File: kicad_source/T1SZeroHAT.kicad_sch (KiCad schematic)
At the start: 35 parts, among them CN1 RASPI-IO, CN2 XY2500R-F-3.81-4P, CN3 SM04B-GHS-TB, CN4 SM04B-GHS-TB, SW1 SS-3235S-L3, U1 MCP2518FDT-E/SL, U2 TCAN332GDR, Y1 X1E0000210808

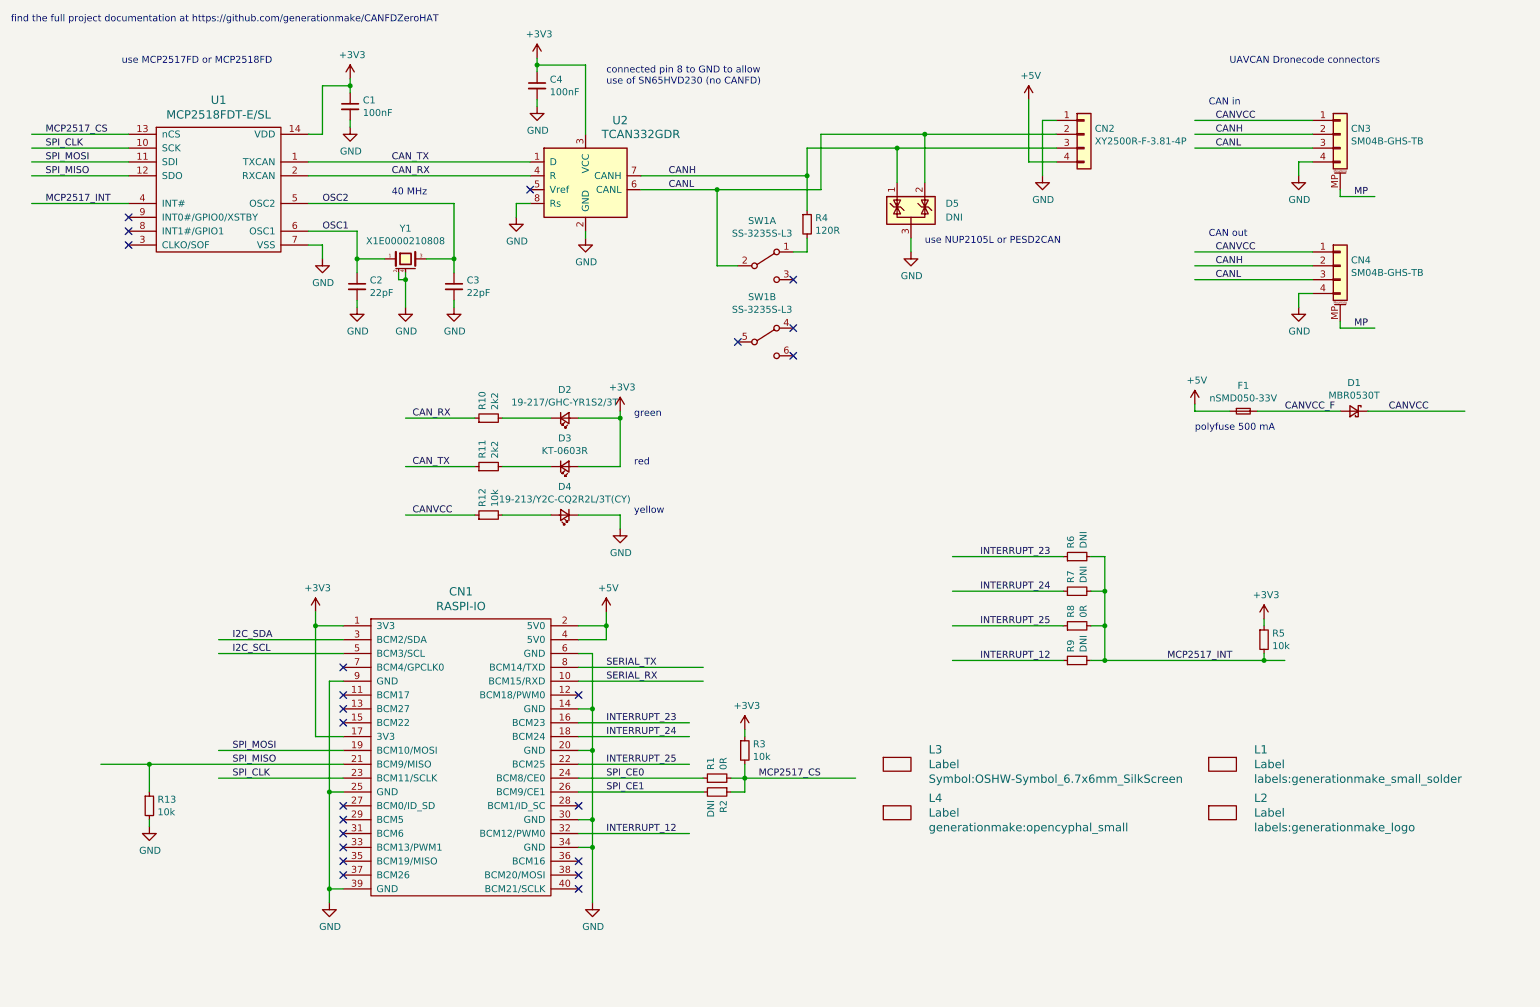
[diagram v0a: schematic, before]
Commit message: added LAN8651 to the schematic
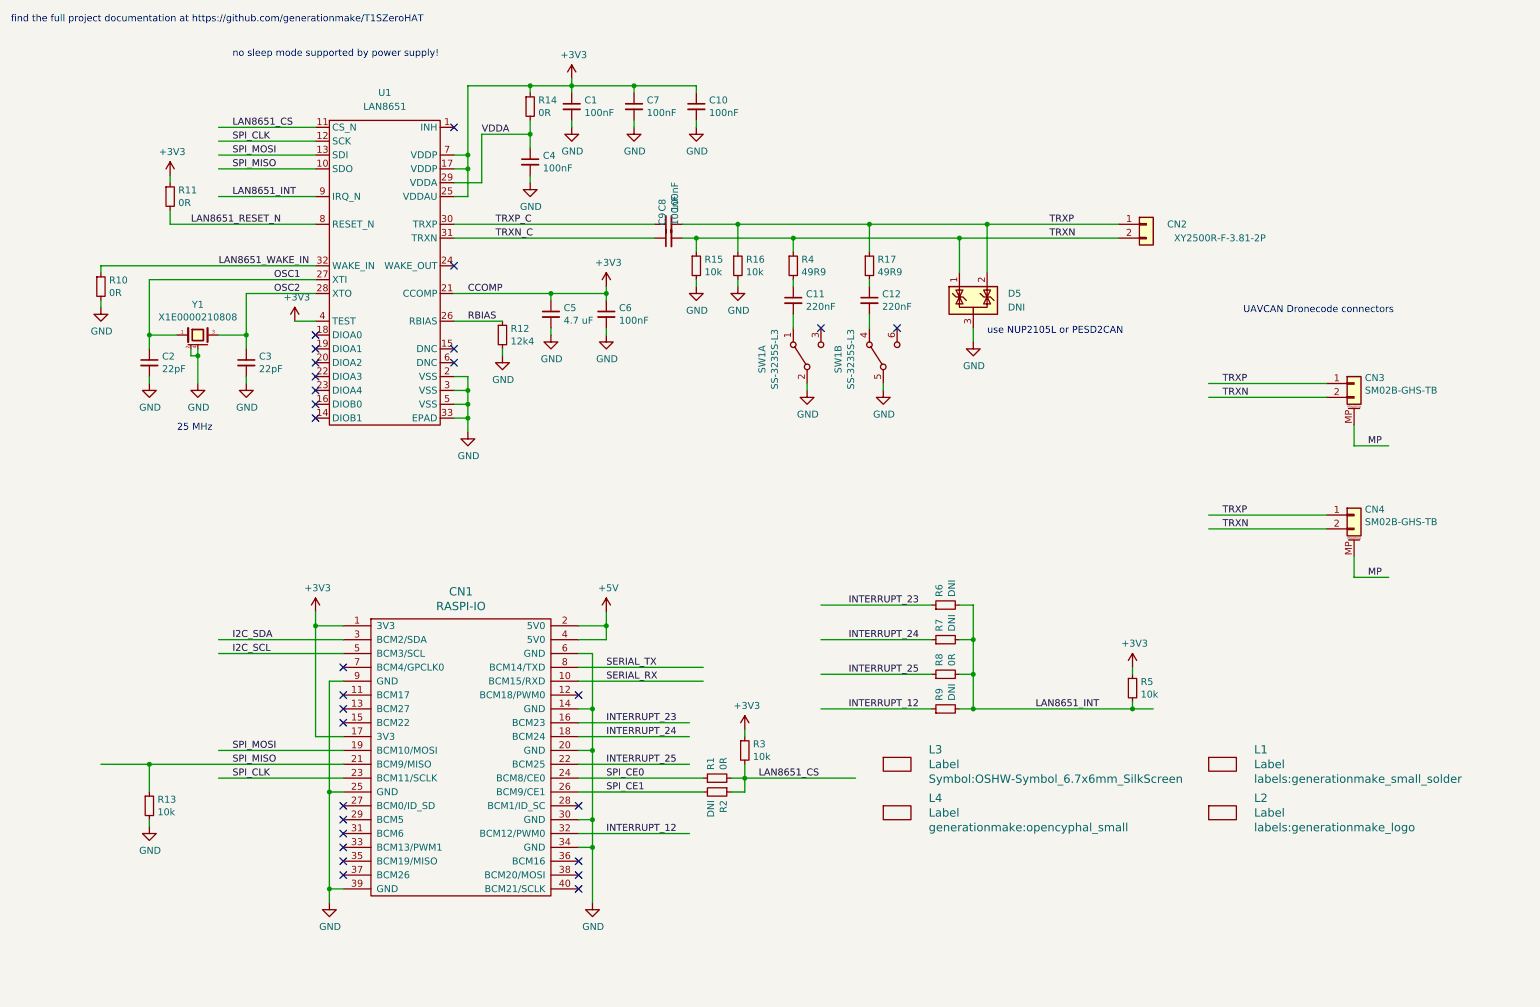
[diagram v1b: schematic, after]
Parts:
- removed D1: MBR0530T, Diode_SMD:D_SOD-123, symbol Device:D_Schottky_Small
- removed D2: 19-217/GHC-YR1S2/3T, LED_SMD:LED_0603_1608Metric, symbol Device:LED_Small
- removed D3: KT-0603R, LED_SMD:LED_0603_1608Metric, symbol Device:LED_Small
- removed D4: 19-213/Y2C-CQ2R2L/3T(CY), LED_SMD:LED_0603_1608Metric, symbol Device:LED_Small
- removed F1: nSMD050-33V, Fuse:Fuse_1206_3216Metric, symbol Device:Fuse_Small
- removed U1: MCP2518FDT-E/SL, Package_SO:SOIC-14_3.9x8.7mm_P1.27mm, symbol CANFDZeroHAT-rescue:MCP2517FD-IC_transceiver_can
- removed U2: TCAN332GDR, Package_SO:SOIC-8_3.9x4.9mm_P1.27mm, symbol Interface_CAN_LIN:SN65HVD230
- added C10, C6, C7, C8, C9: 100nF, Capacitor_SMD:C_0603_1608Metric, symbol Device:C_Small
- added C11, C12: 220nF, Capacitor_SMD:C_0603_1608Metric, symbol Device:C_Small
- added C5: 4.7 uF, Capacitor_SMD:C_0603_1608Metric, symbol Device:C_Small
- added R14: 0R, Resistor_SMD:R_0603_1608Metric, symbol Device:R_Small
- added R15, R16: 10k, Resistor_SMD:R_0603_1608Metric, symbol Device:R_Small
- added R17: 49R9, Resistor_SMD:R_0603_1608Metric, symbol Device:R_Small
- added U1: LAN8651, Package_DFN_QFN:QFN-32-1EP_5x5mm_P0.5mm_EP3.45x3.45mm, symbol generationmake:LAN8651
- CN2: value XY2500R-F-3.81-4P -> XY2500R-F-3.81-2P; footprint Connector_Phoenix_MC:PhoenixContact_MC_1,5_4-G-3.81_1x04_P3.81mm_Horizontal -> Connector_Phoenix_MC:PhoenixContact_MC_1,5_2-G-3.81_1x02_P3.81mm_Horizontal; symbol Connector_Generic:Conn_01x04 -> Connector_Generic:Conn_01x02; LCSC C880583 -> (none)
- CN3, CN4: value SM04B-GHS-TB -> SM02B-GHS-TB; footprint Connector_JST:JST_GH_SM04B-GHS-TB_1x04-1MP_P1.25mm_Horizontal -> Connector_JST:JST_GH_SM02B-GHS-TB_1x02-1MP_P1.25mm_Horizontal; symbol Connector_Generic_MountingPin:Conn_01x04_MountingPin -> Connector_Generic_MountingPin:Conn_01x02_MountingPin; LCSC C189895 -> (none)
- R10, R11: value 2k2 -> 0R; LCSC C4190 -> C2889381
- R12: value 10k -> 12k4; LCSC C25804 -> (none)
- R4: value 120R -> 49R9; LCSC C22787 -> (none)
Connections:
- net CAN_TX is gone; now on net +3.3V: R11.1
- net +3.3V: now also C10.1, C5.1, C6.1, C7.1, R14.1, U1.17 (VDDP), U1.21 (CCOMP), U1.25 (VDDAU), U1.4 (TEST), U1.7 (VDDP); no longer C4.1
- net +5V: no longer CN2.4 (Pin_4)
- net GND: now also R10.2, R12.2, SW1.2 (B), SW1.5 (B), C10.2, C5.2, C6.2, C7.2, R15.2, R16.2, U1.2 (VSS), U1.3 (VSS), U1.33 (EPAD), U1.5 (VSS); no longer CN2.1 (Pin_1), CN3.4 (Pin_4), CN4.4 (Pin_4)
- net OSC1: now also U1.27 (XTI)
- net OSC2: now also U1.28 (XTO)
- net SPI_CLK: now also U1.12 (SCK)
- net SPI_MISO: now also U1.10 (SDO)
- net SPI_MOSI: now also U1.13 (SDI)
- net at R4.2: now also C11.1; no longer SW1.1 (A)
- net LAN8651_RESET_N: now reaches R11.2
- net LAN8651_RESET_N: now also U1.8 (RESET_N)
- net at SW1.4 (A): now also C12.2
- net CANH renamed TRXN
- net TRXN: now also CN2.2 (Pin_2), C9.2, R15.1; no longer CN2.3 (Pin_3)
- removed net CANL: CN2.2 (Pin_2), CN3.3 (Pin_3), CN4.3 (Pin_3), D5.2 (K), SW1.2 (B)
- net CANVCC renamed TRXP
- net TRXP: now also CN2.1 (Pin_1), D5.2 (K), C8.2, R16.1, R17.1; no longer R12.1
- net CAN_RX renamed LAN8651_WAKE_IN
- net LAN8651_WAKE_IN: now also U1.32 (WAKE_IN)
- net MCP2517_CS renamed LAN8651_CS
- net LAN8651_CS: now also U1.11 (CS_N)
- net MCP2517_INT renamed LAN8651_INT
- net LAN8651_INT: now also U1.9 (IRQ_N)
- new net: C11.2, SW1.1 (A)
- new net: C12.1, R17.2
- new net RBIAS: R12.1, U1.26 (RBIAS)
- new net TRXN_C: C9.1, U1.31 (TRXN)
- new net TRXP_C: C8.1, U1.30 (TRXP)
- new net VDDA: C4.1, R14.2, U1.29 (VDDA)
- no-connect marks 23 -> 28
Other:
- note added: "25 MHz"
- note added: "find the full project documentation at https://github.com/generationmake/T1SZeroHAT"
- note added: "no sleep mode supported by power supply!"
- note removed: "40 MHz"
- note removed: "CAN in"
- note removed: "CAN out"
- note removed: "connected pin 8 to GND to allow use of SN65HVD230 (no CANFD)"
- note removed: "find the full project documentation at https://github.com/generationmake/CANFDZeroHAT"
- note removed: "green"
- note removed: "polyfuse 500 mA"
- note removed: "red"
- note removed: "use MCP2517FD or MCP2518FD"
- note removed: "yellow"
- title: CANFDZeroHAT -> T1SZeroHAT
- moved on the sheet: C1, C2, C3, D5, R4, R5, R6, R7, R8, R9, SW1A, SW1B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

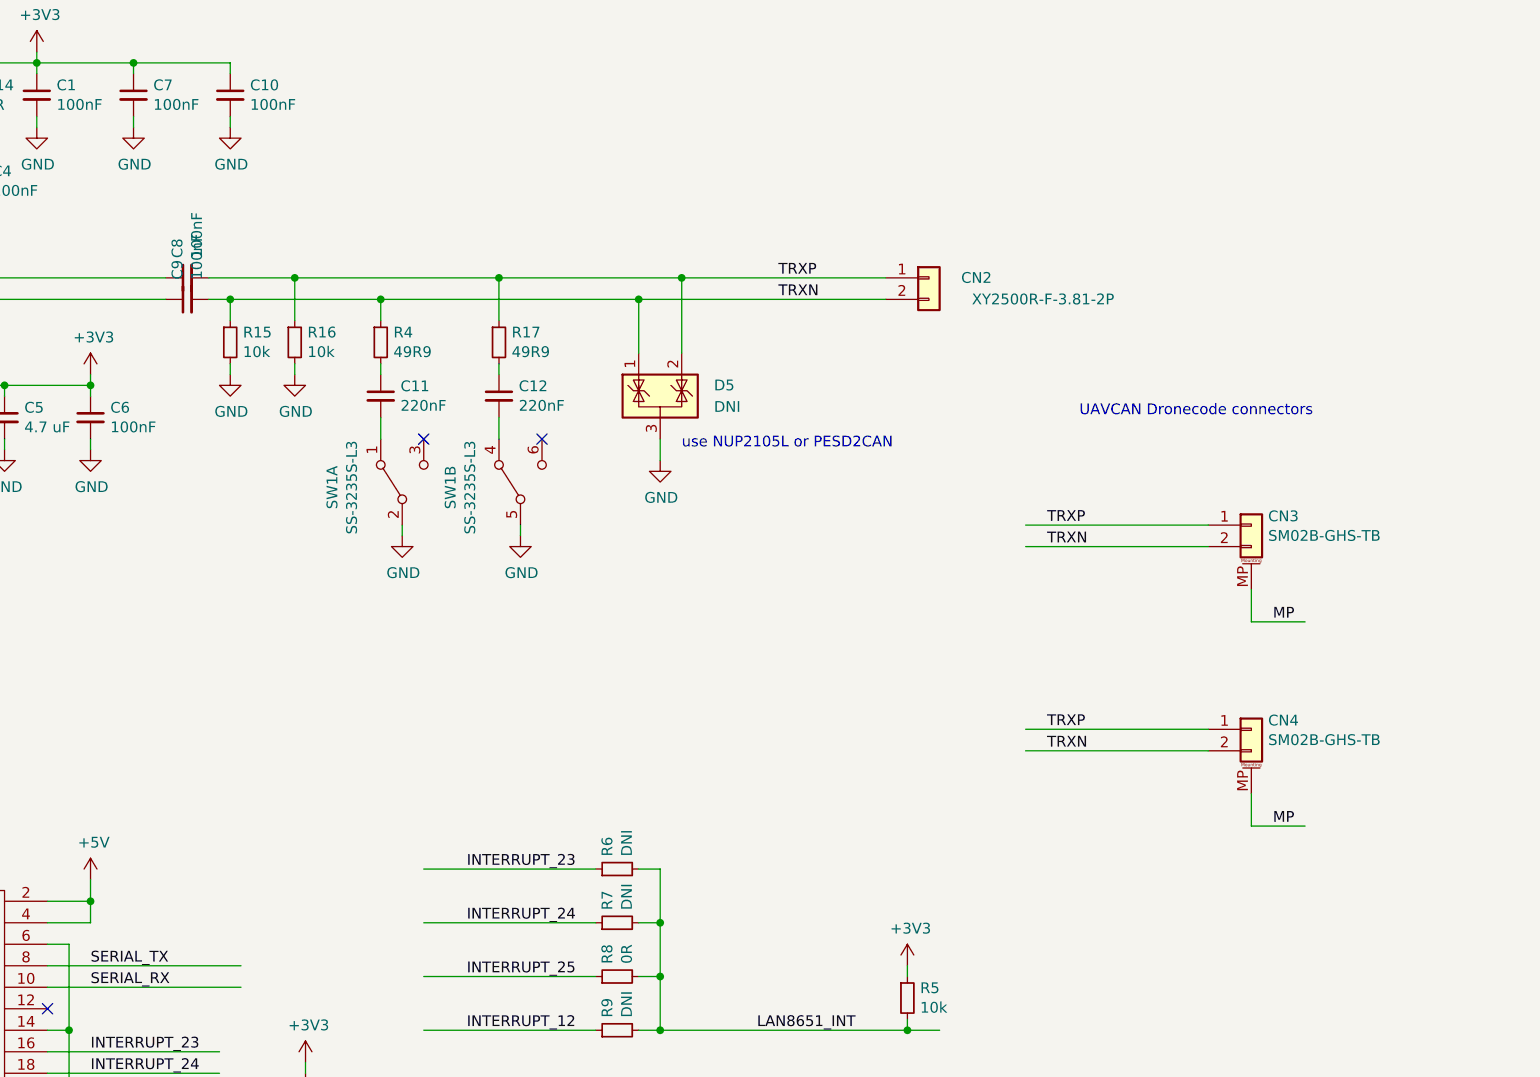
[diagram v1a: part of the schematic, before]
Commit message: added common mode choke on ethernet lines
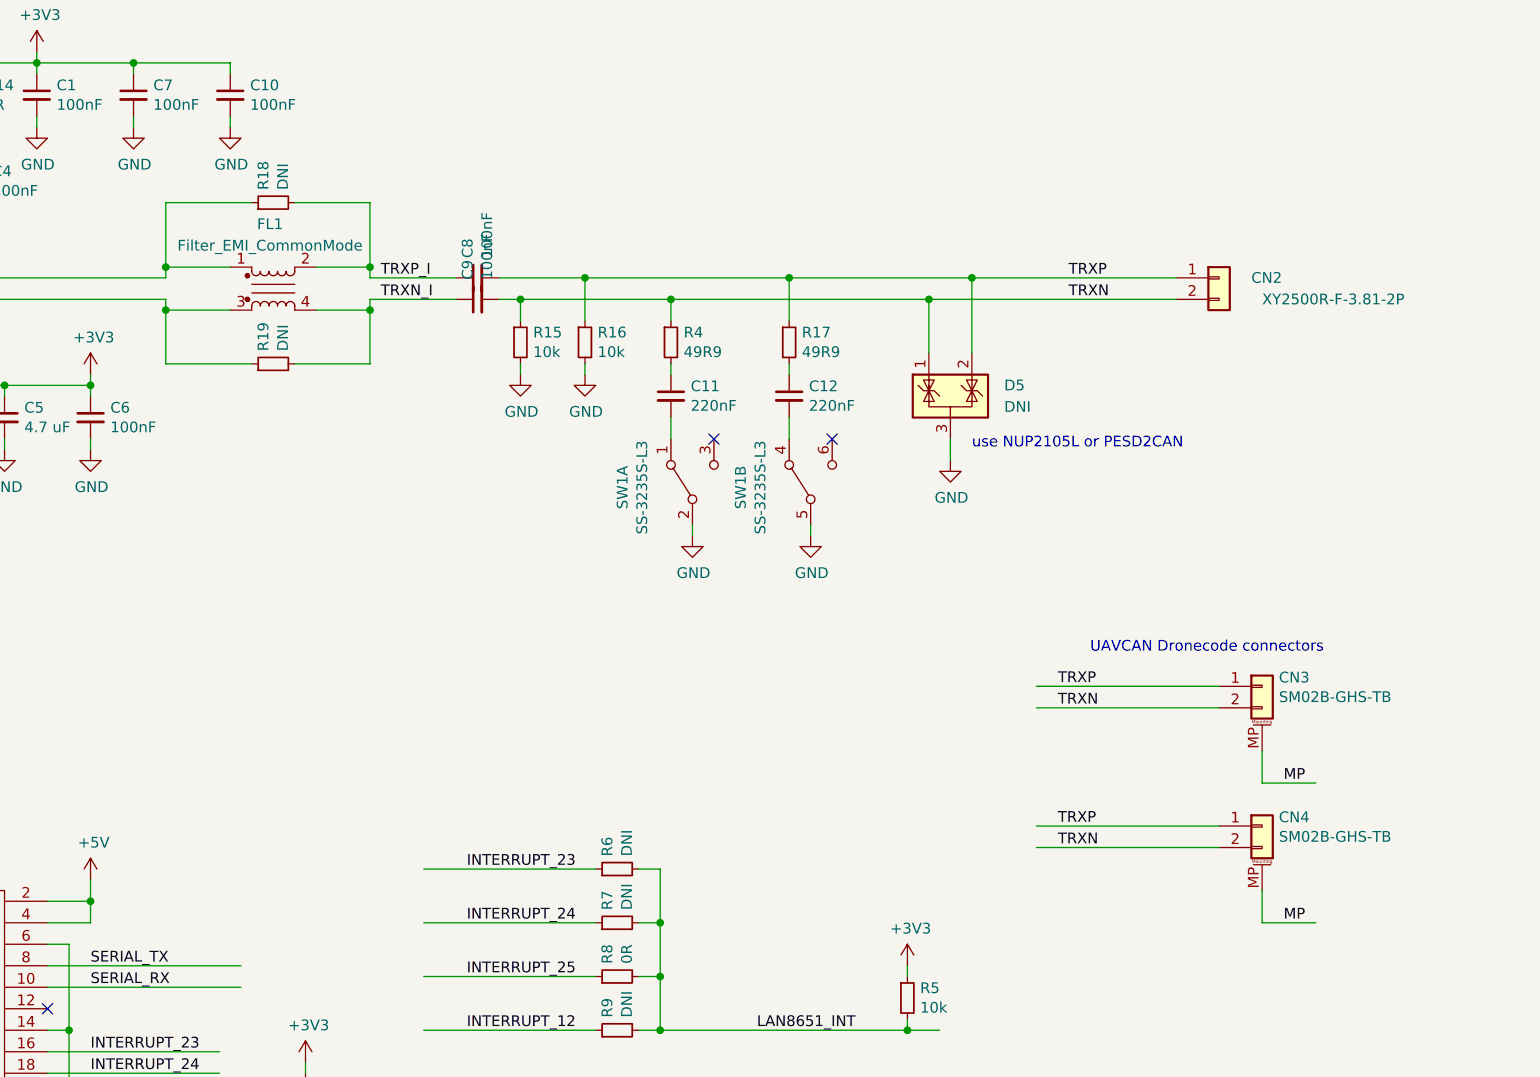
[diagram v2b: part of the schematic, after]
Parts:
- added FL1: Filter_EMI_CommonMode, Filter:Filter_Bourns_SRF0905_6.0x9.2mm, symbol Device:Filter_EMI_CommonMode
- added R18, R19: DNI, Resistor_SMD:R_0603_1608Metric, symbol Device:R_Small
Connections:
- net TRXN_C: now also FL1.3, R19.1; no longer C9.1
- net TRXP_C: now also FL1.1, R18.1; no longer C8.1
- new net TRXN_I: C9.1, FL1.4, R19.2
- new net TRXP_I: C8.1, FL1.2, R18.2
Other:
- moved on the sheet: C11, C12, C8, C9, CN2, CN3, CN4, D5, R15, R16, R17, R4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

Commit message: made first draft of layout
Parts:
- FL1: symbol Device:Filter_EMI_CommonMode -> Device:Filter_EMI_LL_1423
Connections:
- net +3.3V: no longer C5.1, C6.1, U1.21 (CCOMP)
- net TRXN_C: now also FL1.1; no longer FL1.3
- net TRXP_C: now also FL1.2; no longer FL1.1
- net TRXP_I: now also FL1.3; no longer FL1.2
- new net CCOMP: C5.1, C6.1, U1.21 (CCOMP)
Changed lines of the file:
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@@
   (junction (at 96.52 82.55) (diameter 0) (color 0 0 0 0)
-  )
-  (junction (at 121.92 64.77) (diameter 0) (color 0 0 0 0)
   )
   (junction (at 130.81 50.8) (diameter 0) (color 0 0 0 0)
@@
     (stroke (width 0) (type default) (color 0 0 0 0))
   )
-  (wire (pts (xy 121.92 63.5) (xy 121.92 64.77))
-    (stroke (width 0) (type default) (color 0 0 0 0))
-  )
   (wire (pts (xy 130.81 54.61) (xy 130.81 55.88))
     (stroke (width 0) (type default) (color 0 0 0 0))
@@
     (pin "2")
   )
-  (symbol (lib_id "power:+3.3V") (at 121.92 63.5 0) (unit 1)
-    (in_bom yes) (on_board yes)
-    (property "Reference" "#PWR015" (id 0) (at 121.92 67.31 0)
-      (effects (font (size 1.27 1.27)) hide)
-    )
-    (property "Value" "+3V3" (id 1) (at 122.301 59.1058 0))
-    (property "Footprint" "" (id 2) (at 121.92 63.5 0))
-    (property "Datasheet" "" (id 3) (at 121.92 63.5 0))
-    (pin "1")
-  )
   (symbol (lib_id "Device:R_Small") (at 143.51 43.18 90) (unit 1)
     (in_bom no) (on_board yes)
@@
     (pin "1")
   )
-  (symbol (lib_id "Device:Filter_EMI_CommonMode") (at 143.51 53.34 0) (unit 1)
+  (symbol (lib_id "Device:Filter_EMI_LL_1423") (at 143.51 53.34 0) (unit 1)
     (in_bom yes) (on_board yes) (fields_autoplaced)
     (property "Reference" "FL1" (id 0) (at 143.129 45.72 0))
     (property "Value" "Filter_EMI_CommonMode" (id 1) (at 143.129 48.26 0))
-    (property "Footprint" "Filter:Filter_Bourns_SRF0905_6.0x9.2mm" (id 2) (at 143.51 52.324 0)
-      (effects (font (size 1.27 1.27)) hide)
-    )
-    (property "Datasheet" "~" (id 3) (at 143.51 52.324 0)
+    (property "Footprint" "Filter:Filter_Bourns_SRF0905_6.0x9.2mm" (id 2) (at 143.51 59.69 0)
+      (effects (font (size 1.27 1.27)) hide)
+    )
+    (property "Datasheet" "~" (id 3) (at 143.51 52.324 90)
       (effects (font (size 1.27 1.27)) hide)
     )
@@
       (reference "#PWR014") (unit 1) (value "GND") (footprint "")
     )
-    (path "/182c04d8-d89c-4d1a-921c-0f9a1a4cf4c5"
-      (reference "#PWR015") (unit 1) (value "+3V3") (footprint "")
-    )
     (path "/ba6f2d3a-66f0-4b32-8dad-e6053c021eab"
